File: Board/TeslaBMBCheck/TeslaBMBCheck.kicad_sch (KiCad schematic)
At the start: 31 parts, among them J1 TESLA_BMS, J9 ICSP, Q1 IRLML2244, Q2 BSS138, U1 USBLC6, U2 PIC18F2480-ISO, Y1 10 MHz

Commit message: Minor improvements
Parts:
- R6: value 22 -> 15
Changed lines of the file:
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@@
 			)
 		)
-		(property "Value" "22"
+		(property "Value" "15"
 			(at 65.532 58.547 0)
 			(effects

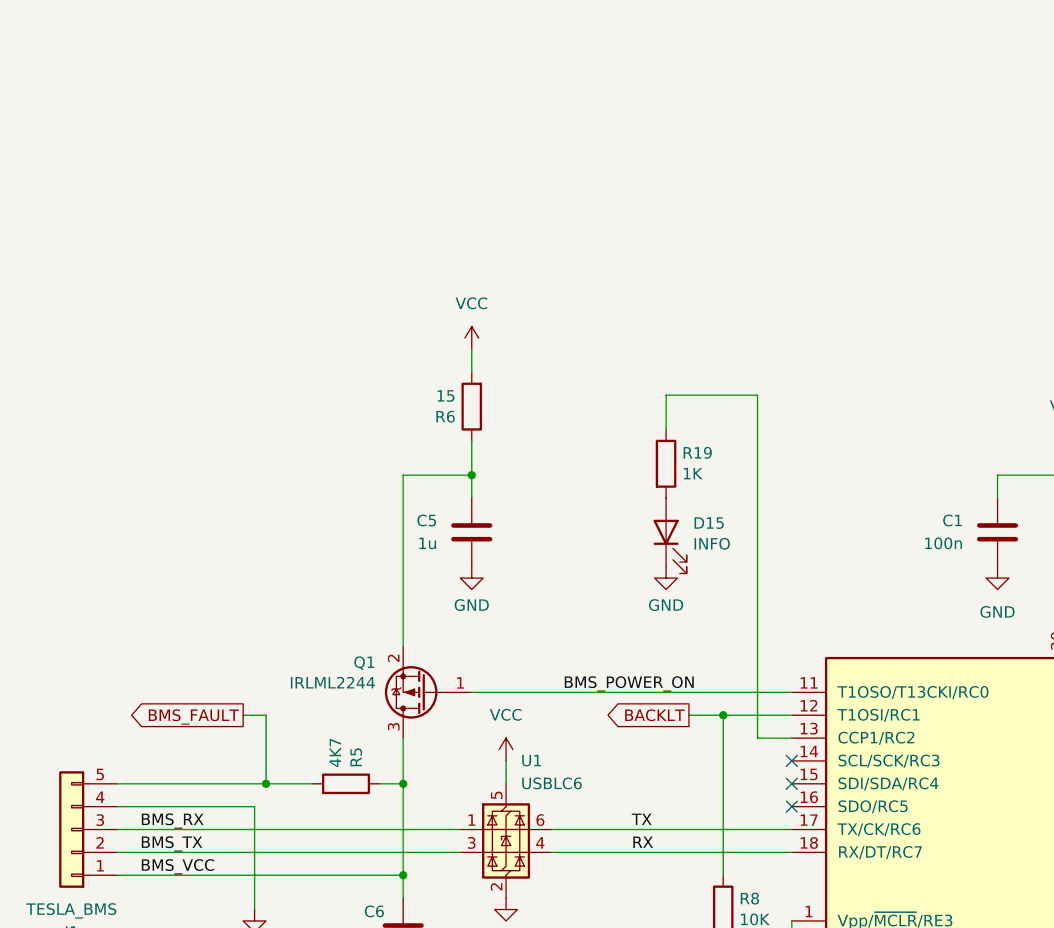
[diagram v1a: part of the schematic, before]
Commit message: Adds charging relais. New layout.
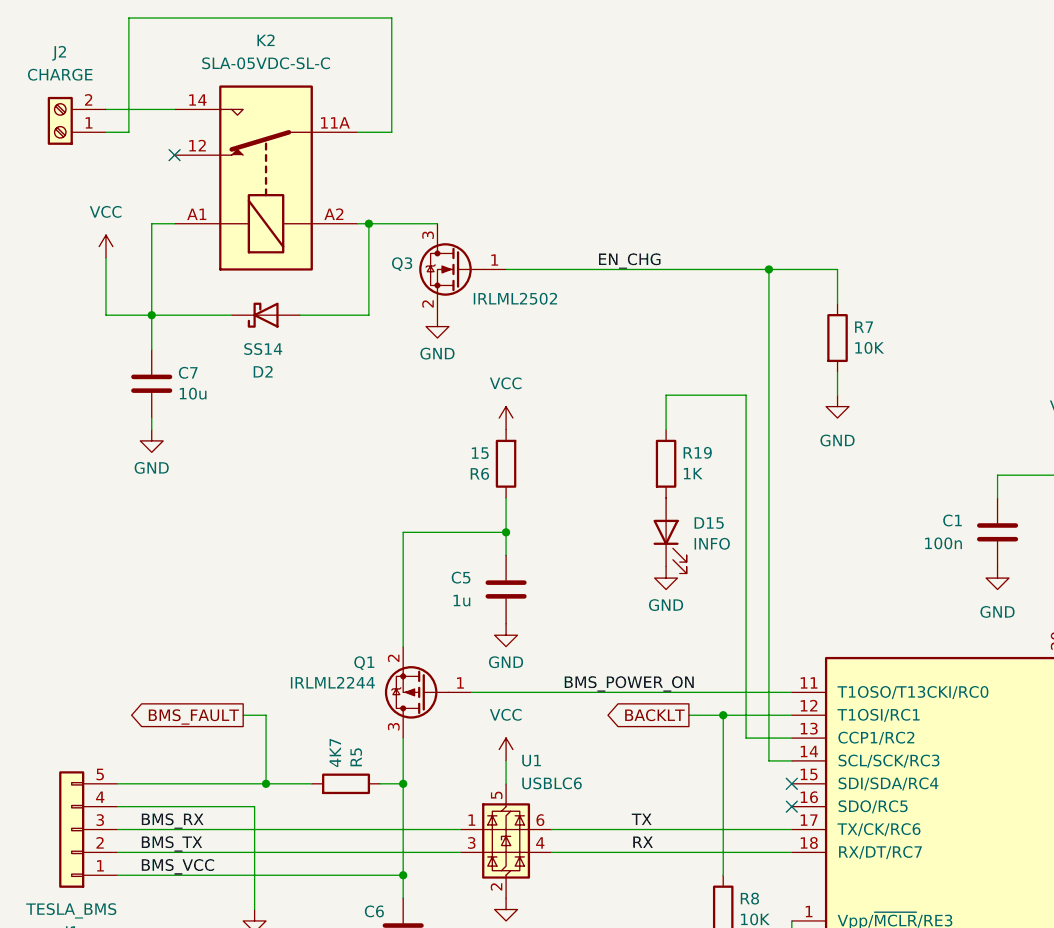
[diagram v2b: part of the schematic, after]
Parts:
- added C7: 10u, Capacitor_SMD:C_1206_3216Metric, symbol Device:C
- added D2: SS14, Diode_SMD:D_SMA, symbol Device:D_Schottky
- added J2: CHARGE, spetry:KF7.62_2P, symbol Connector:Screw_Terminal_01x02
- added K2: SLA-05VDC-SL-C, Relay_THT:Relay_SPDT_RAYEX-L90, symbol Relay:RAYEX-L90
- added Q3: IRLML2502, Package_TO_SOT_SMD:SOT-23, symbol Transistor_FET:BSS138
- added R7: 10K, Resistor_SMD:R_0805_2012Metric, symbol Device:R
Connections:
- net GND: now also C7.2, Q3.2 (S), R7.2
- net VCC: now also C7.1, D2.1 (K), K2.A1
- net EN_CHG: now reaches U2.14 (SCL/SCK/RC3)
- net EN_CHG: now also Q3.1 (G), R7.1
- new net: D2.2 (A), K2.A2, Q3.3 (D)
- new net: J2.1 (Pin_1), K2.11A, K2.11B
- new net: J2.2 (Pin_2), K2.14
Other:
- moved on the sheet: C5, R6
